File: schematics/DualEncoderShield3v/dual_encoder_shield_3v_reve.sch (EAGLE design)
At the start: 40 parts, among them J1 2X6 FEMALE, M1 ARDUINO_R3_ICSP, Q1 ON_SEMI_BSS138ON_SEMI_BSS138_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, Q2 ON_SEMI_BSS138ON_SEMI_BSS138_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, Q3 ON_SEMI_BSS138ON_SEMI_BSS138_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, Q4 ON_SEMI_BSS138ON_SEMI_BSS138_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, U1 74LVC1G14GW, U2 74LVC1G14GW

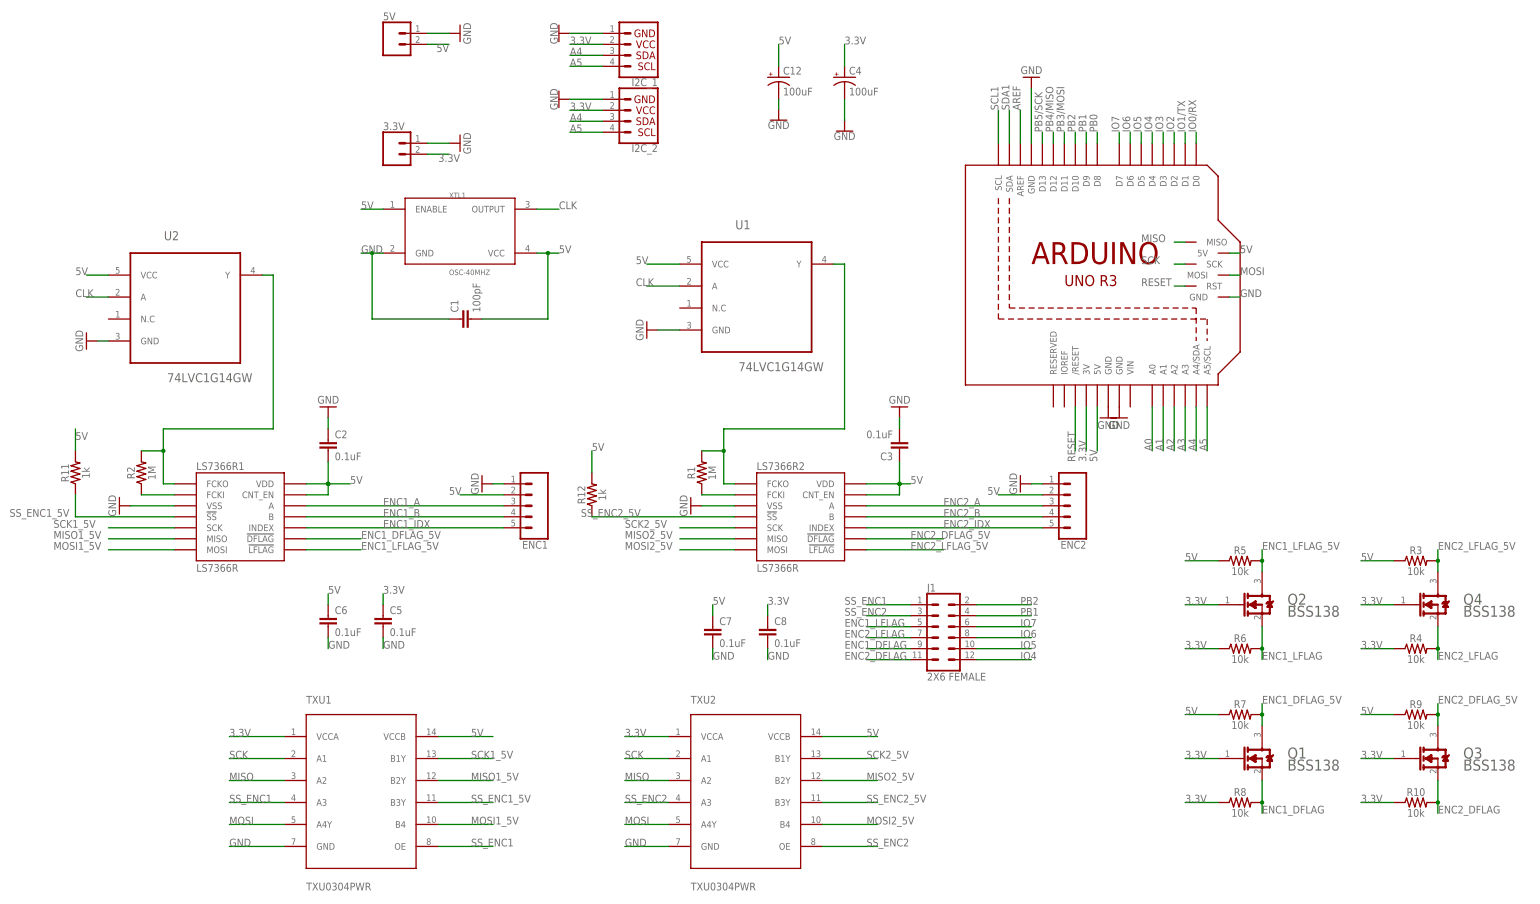
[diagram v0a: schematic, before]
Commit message: Update readme, sketches, and schematics
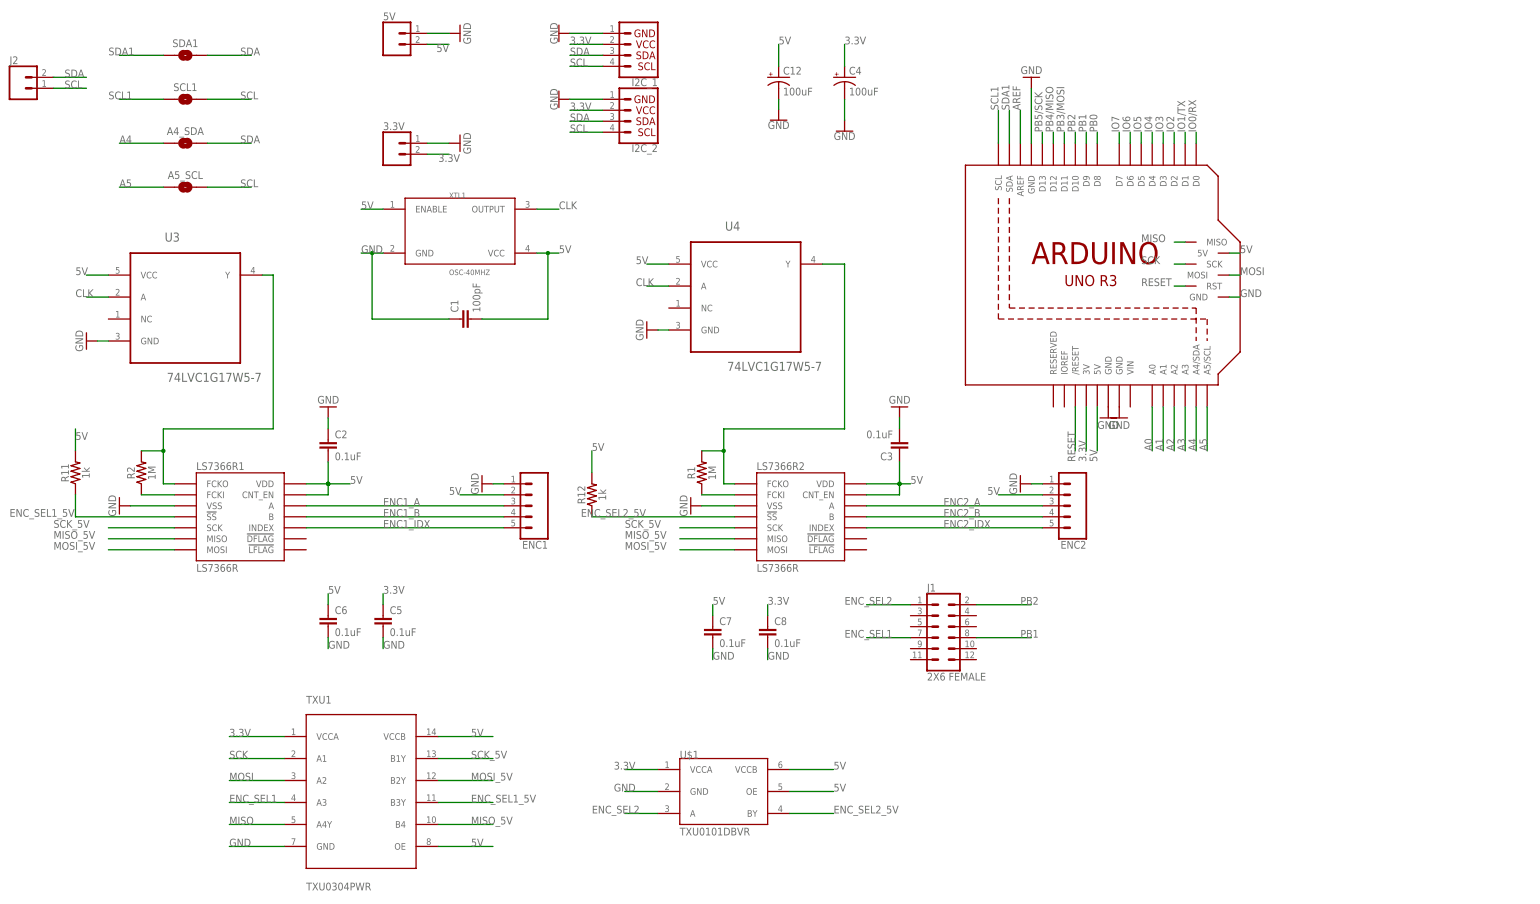
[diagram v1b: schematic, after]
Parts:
- removed Q1, Q2, Q3, Q4: ON_SEMI_BSS138ON_SEMI_BSS138_0_0, ON Semi - BSS138:ON_SEMI_BSS138ON_SEMI_BSS138_0_0
- removed R10, R3, R4, R5, R6, R7, R8, R9: 10k, SparkFun-Resistors:10KOHM-0603-1/10W-1%
- removed TXU2: TXU0304PWR, steveo:TXU0304PWR
- removed U1, U2: 74LVC1G14GW, 74LVC1G14GW:74LVC1G14GW
- added A4_SDA, A5_SCL, SCL1, SDA1: JUMPER-SMT_2_NO_NO-SILK, SparkFun-Jumpers:JUMPER-SMT_2_NO_NO-SILK
- added J2: (no value), SparkFun-Connectors:CONN_02
- added U$1: TXU0101DBVR, steveo:TXU0101DBVR
- added U3, U4: 74LVC1G17W5-7, 74LVC1G17W5-7:74LVC1G17W5-7
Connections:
- net SS_ENC1_5V renamed ENC_SEL1_5V
- removed net ENC1_DFLAG: J1.9, Q1.S, R8.2
- removed net ENC1_DFLAG_5V: LS7366R1.!DFLAG, Q1.D, R7.2
- removed net ENC1_LFLAG: J1.5, Q2.S, R6.2
- removed net ENC1_LFLAG_5V: LS7366R1.!LFLAG, Q2.D, R5.2
- removed net ENC2_DFLAG: J1.11, Q3.S, R10.2
- removed net ENC2_DFLAG_5V: LS7366R2.!DFLAG, Q3.D, R9.2
- removed net ENC2_LFLAG: J1.7, Q4.S, R4.2
- removed net ENC2_LFLAG_5V: LS7366R2.!LFLAG, Q4.D, R3.2
- removed net MISO1_5V: LS7366R1.MISO, TXU1.B2Y
- removed net MISO2_5V: LS7366R2.MISO, TXU2.B2Y
- removed net MOSI1_5V: LS7366R1.MOSI, TXU1.B4
- removed net MOSI2_5V: LS7366R2.MOSI, TXU2.B4
- removed net SCK1_5V: LS7366R1.SCK, TXU1.B1Y
- removed net SCK2_5V: LS7366R2.SCK, TXU2.B1Y
- removed net SS_ENC1: J1.1, TXU1.A3, TXU1.OE
- removed net SS_ENC2: J1.3, TXU2.A3, TXU2.OE
- removed net SS_ENC2_5V: LS7366R2.!SS, R12.1, TXU2.B3Y
- new net ENC_SEL1: J1.7, TXU1.A3
- new net ENC_SEL2: J1.1, U$1.A
- new net ENC_SEL2_5V: LS7366R2.!SS, R12.1, U$1.BY
- new net MISO_5V: LS7366R1.MISO, LS7366R2.MISO, TXU1.B4
- new net MOSI_5V: LS7366R1.MOSI, LS7366R2.MOSI, TXU1.B2Y
- new net SCK_5V: LS7366R1.SCK, LS7366R2.SCK, TXU1.B1Y
- new net SCL: A5_SCL.2, I2C_1.4, I2C_2.4, J2.1, SCL1.2
- new net SDA: A4_SDA.2, I2C_1.3, I2C_2.3, J2.2, SDA1.2
- net 3.3V: now also U$1.VCCA; no longer Q1.G, Q2.G, Q3.G, Q4.G, R10.1, R4.1, R6.1, R8.1, TXU2.VCCA
- net 5V: now also TXU1.OE, U$1.OE, U$1.VCCB, U3.VCC, U4.VCC; no longer R3.1, R5.1, R7.1, R9.1, TXU2.VCCB, U1.VCC, U2.VCC
- net A4: now also A4_SDA.1; no longer I2C_1.3, I2C_2.3
- net A5: now also A5_SCL.1; no longer I2C_1.4, I2C_2.4
- net CLK: now also U3.A, U4.A; no longer U1.A, U2.A
- net GND: now also U$1.GND, U3.GND, U4.GND; no longer TXU2.GND, U1.GND, U2.GND
- net IO4: no longer J1.12
- net IO5: no longer J1.10
- net IO6: no longer J1.8
- net IO7: no longer J1.6
- net MISO: now also TXU1.A4Y; no longer TXU1.A2, TXU2.A2
- net MOSI: now also TXU1.A2; no longer TXU1.A4Y, TXU2.A4Y
- net N$10: now also U3.Y; no longer U2.Y
- net N$8: now also U4.Y; no longer U1.Y
- net PB1: now also J1.8; no longer J1.4
- net SCK: no longer TXU2.A1
- net SCL1: now also SCL1.1
- net SDA1: now also SDA1.1
